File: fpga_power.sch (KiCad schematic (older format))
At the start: 25 parts, among them J81 JTAG, J82 Jumper, SW81 nConfig, U8 10M16DCF256I7G_mk3pinstest

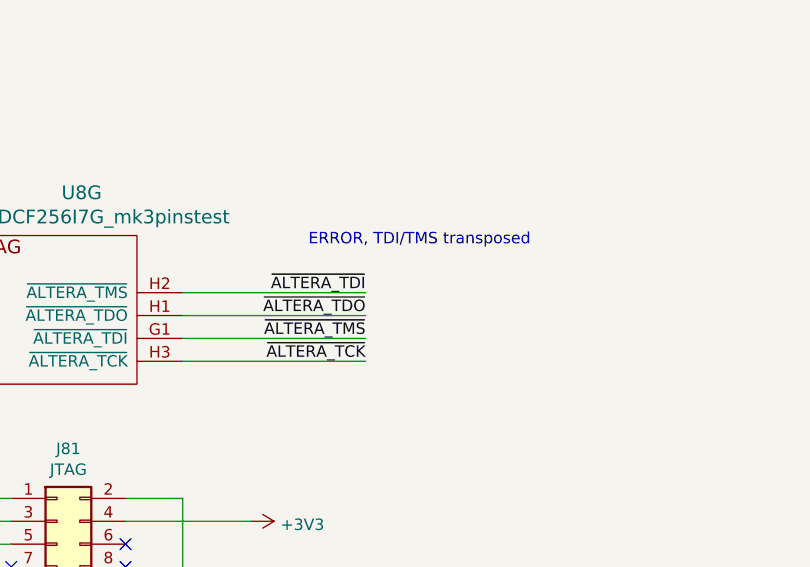
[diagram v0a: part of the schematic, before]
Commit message: Mk.3 fixes and new 68000 expansion board
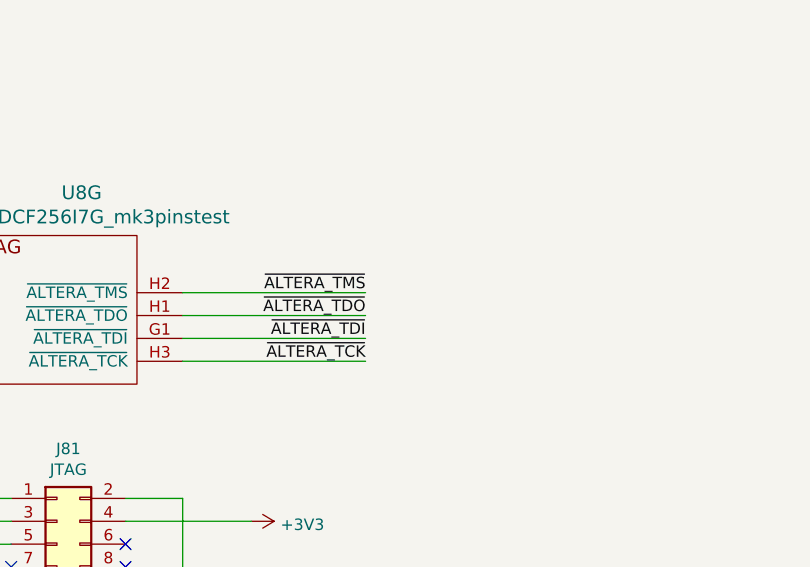
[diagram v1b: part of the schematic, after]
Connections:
- net ~ALTERA_TDI~: now also U8.G1 (~ALTERA_TDI~); no longer U8.H2 (~ALTERA_TMS~)
- net ~ALTERA_TMS~: now also U8.H2 (~ALTERA_TMS~); no longer U8.G1 (~ALTERA_TDI~)
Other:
- note removed: "ERROR, TDI/TMS transposed"
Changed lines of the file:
@@
 Sheet 10 11
 Title "Mk.3 Blitter FPGA development board"
-Date "2021-05-08"
-Rev "3.00"
+Date "2021-08-14"
+Rev "3.03"
 Comp "Dossytronics"
-Comment1 ""
+Comment1 "fixed: clk/sysd0, jtag, u22 footprint"
 Comment2 ""
 Comment3 ""
@@
 	1    0    0    -1
 $EndComp
-Text Label 3400 5200 2    50   ~ 0
+Text Label 3400 5400 2    50   ~ 0
 ~ALTERA_TDI~
 Text Label 3400 5300 2    50   ~ 0
 ~ALTERA_TDO~
-Text Label 3400 5400 2    50   ~ 0
+Text Label 3400 5200 2    50   ~ 0
 ~ALTERA_TMS~
 Text Label 3400 5500 2    50   ~ 0
@@
 Wire Wire Line
 	6500 5900 6750 5900
-Text Notes 3150 5000 0    50   ~ 0
-ERROR, TDI/TMS transposed
 $EndSCHEMATC
